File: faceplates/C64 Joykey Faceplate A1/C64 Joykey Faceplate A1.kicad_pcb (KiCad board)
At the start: 2 copper layers, 99.7 x 74.9 mm, 4 parts, among them M1 Mounting, M2 Mounting, M3 Mounting, M4 Mounting

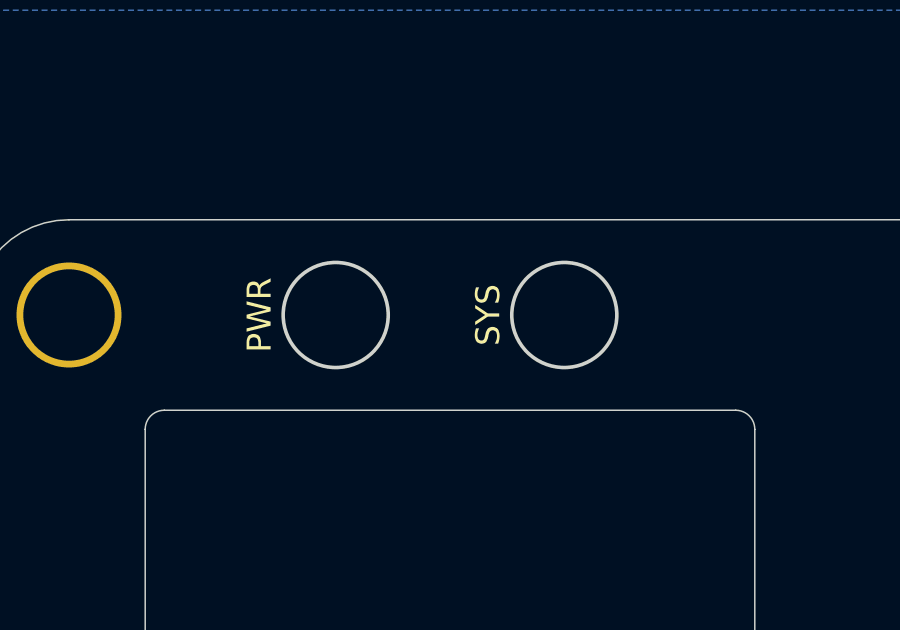
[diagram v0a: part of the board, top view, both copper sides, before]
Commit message: Tweaked faceplates to allow more leeway on LEDs
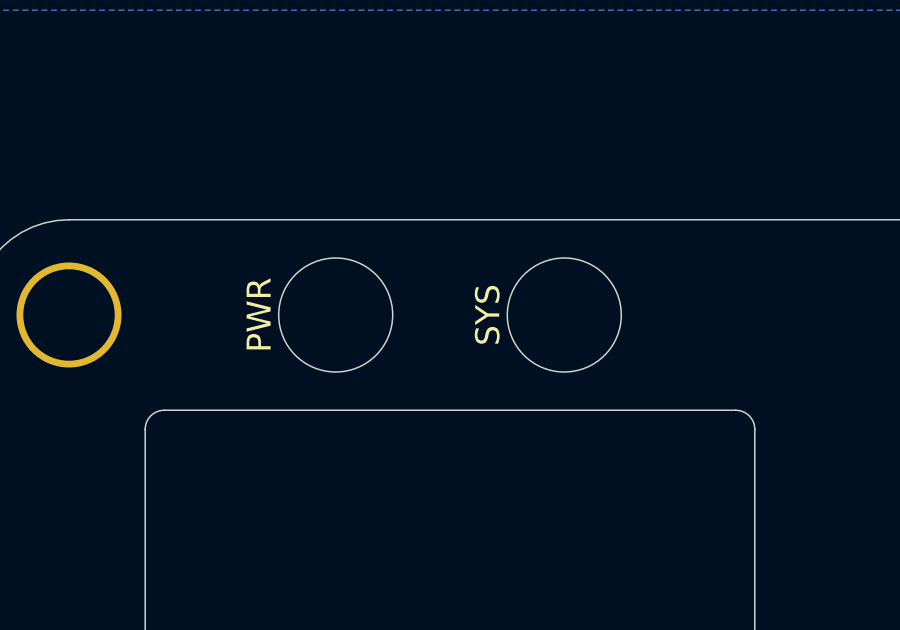
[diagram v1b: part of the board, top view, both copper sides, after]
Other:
- outline, holes or cut-outs redrawn
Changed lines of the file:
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@@
   (general
     (thickness 1.6)
-    (drawings 53)
+    (drawings 49)
     (tracks 0)
     (zones 0)
@@
       (effects (font (size 1 1) (thickness 0.15)))
     )
+    (fp_circle (center 0 0) (end 2.6 0) (layer F.CrtYd) (width 0.05))
     (fp_circle (center 0 0) (end 2 0.8) (layer F.Fab) (width 0.1))
-    (fp_circle (center 0 0) (end 2.6 0) (layer F.CrtYd) (width 0.05))
     (pad 1 thru_hole circle (at 0 0) (size 3.5 3.5) (drill 3.048) (layers *.Cu *.Mask)
       (net 1 "Net-(M1-Pad1)") (solder_mask_margin 0.8))
@@
       (effects (font (size 1 1) (thickness 0.15)))
     )
+    (fp_circle (center 0 0) (end 2 0.8) (layer F.Fab) (width 0.1))
     (fp_circle (center 0 0) (end 2.6 0) (layer F.CrtYd) (width 0.05))
-    (fp_circle (center 0 0) (end 2 0.8) (layer F.Fab) (width 0.1))
     (pad 1 thru_hole circle (at 0 0) (size 3.5 3.5) (drill 3.048) (layers *.Cu *.Mask)
       (net 1 "Net-(M1-Pad1)") (solder_mask_margin 0.8))
@@
       (effects (font (size 1 1) (thickness 0.15)))
     )
+    (fp_circle (center 0 0) (end 2.6 0) (layer F.CrtYd) (width 0.05))
     (fp_circle (center 0 0) (end 2 0.8) (layer F.Fab) (width 0.1))
-    (fp_circle (center 0 0) (end 2.6 0) (layer F.CrtYd) (width 0.05))
     (pad 1 thru_hole circle (at 0 0) (size 3.5 3.5) (drill 3.048) (layers *.Cu *.Mask)
       (net 1 "Net-(M1-Pad1)") (solder_mask_margin 0.8))
@@
       (effects (font (size 1 1) (thickness 0.15)))
     )
+    (fp_circle (center 0 0) (end 2 0.8) (layer F.Fab) (width 0.1))
     (fp_circle (center 0 0) (end 2.6 0) (layer F.CrtYd) (width 0.05))
-    (fp_circle (center 0 0) (end 2 0.8) (layer F.Fab) (width 0.1))
     (pad 1 thru_hole circle (at 0 0) (size 3.5 3.5) (drill 3.048) (layers *.Cu *.Mask)
       (net 1 "Net-(M1-Pad1)") (solder_mask_margin 0.8))
   )
-  (gr_circle (center 153.035 85.725) (end 155.653172 85.725) (layer Dwgs.User) (width 0.05))
-  (gr_circle (center 160.655 85.725) (end 163.273172 85.725) (layer Dwgs.User) (width 0.05))
   (gr_text "PORT 1" (at 200.025 93.98) (layer F.SilkS)
     (effects (font (size 1 1) (thickness 0.15)))
@@
     (effects (font (size 0.8 0.8) (thickness 0.1)))
   )
-  (gr_circle (center 160.655 85.725) (end 162.406 85.725) (layer Edge.Cuts) (width 0.12))
-  (gr_circle (center 153.035 85.725) (end 154.786 85.725) (layer Edge.Cuts) (width 0.12))
-  (gr_circle (center 160.655 85.725) (end 161.925 85.725) (layer B.Mask) (width 2.5))
-  (gr_circle (center 153.035 85.725) (end 154.305 85.725) (layer B.Mask) (width 2.5))
+  (gr_circle (center 160.655 85.725) (end 162.555 85.725) (layer Edge.Cuts) (width 0.05))
+  (gr_circle (center 153.035 85.725) (end 154.935 85.725) (layer Edge.Cuts) (width 0.05))
   (gr_arc (start 189.865 92.075) (end 189.23 92.075) (angle -90) (layer Edge.Cuts) (width 0.05))
   (gr_line (start 189.865 92.71) (end 233.045 92.71) (layer Edge.Cuts) (width 0.05))

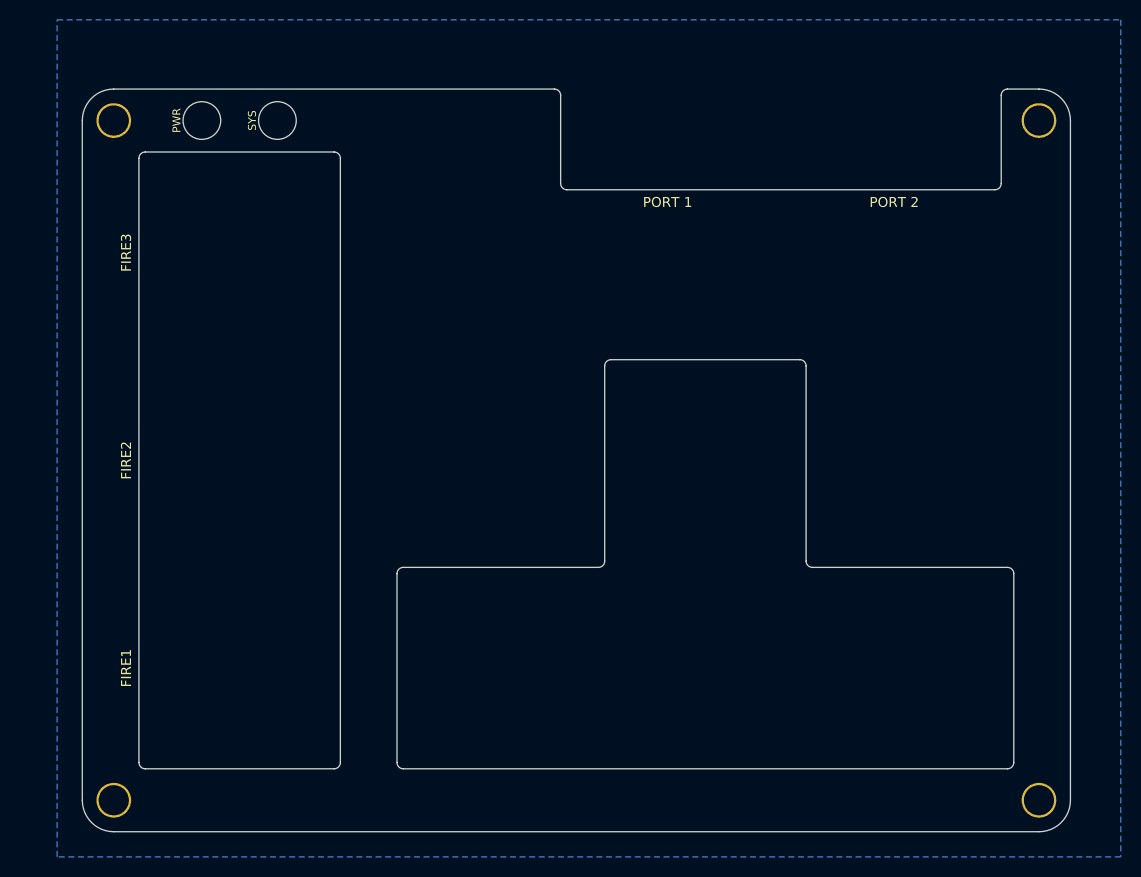
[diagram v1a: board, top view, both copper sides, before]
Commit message: Update to KiCAD8
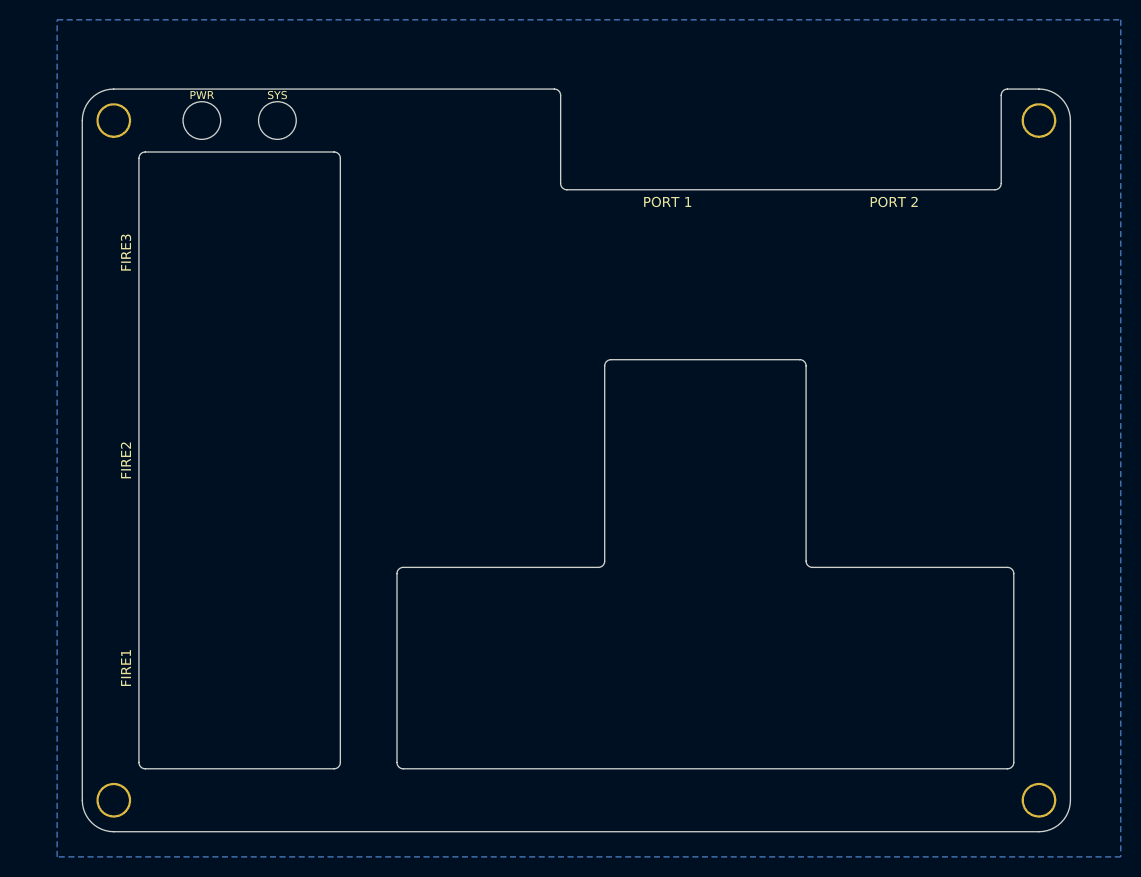
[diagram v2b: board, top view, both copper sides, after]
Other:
- net class Default removed

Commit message: Arcade 2040, and some cleanup
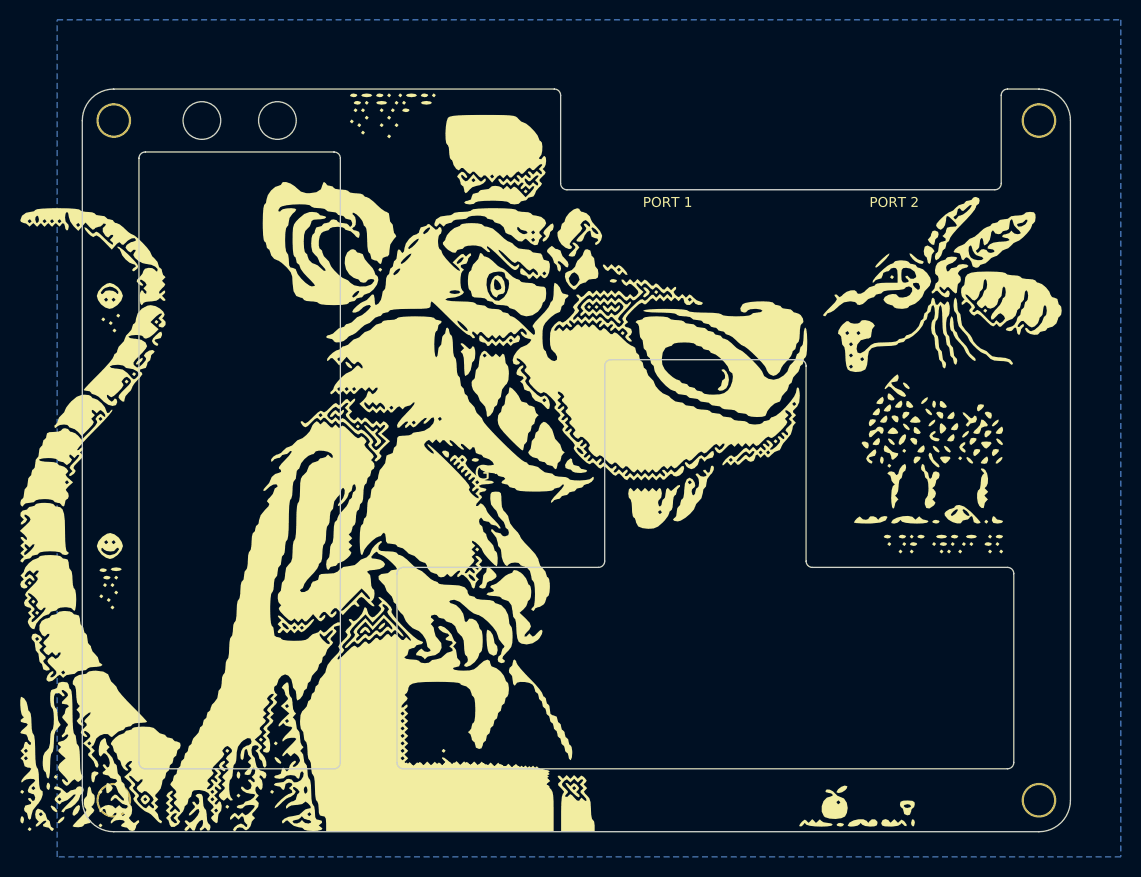
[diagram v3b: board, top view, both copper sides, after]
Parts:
- added G***: LOGO, artwork:rat_a_tat, F.Cu at (182.9, 121.3)
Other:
- board text added: "WayWayWay"
